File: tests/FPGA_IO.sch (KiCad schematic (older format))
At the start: 9 parts, among them U4 iCE40-HX8K-CT256, U7 100 MHz Osc

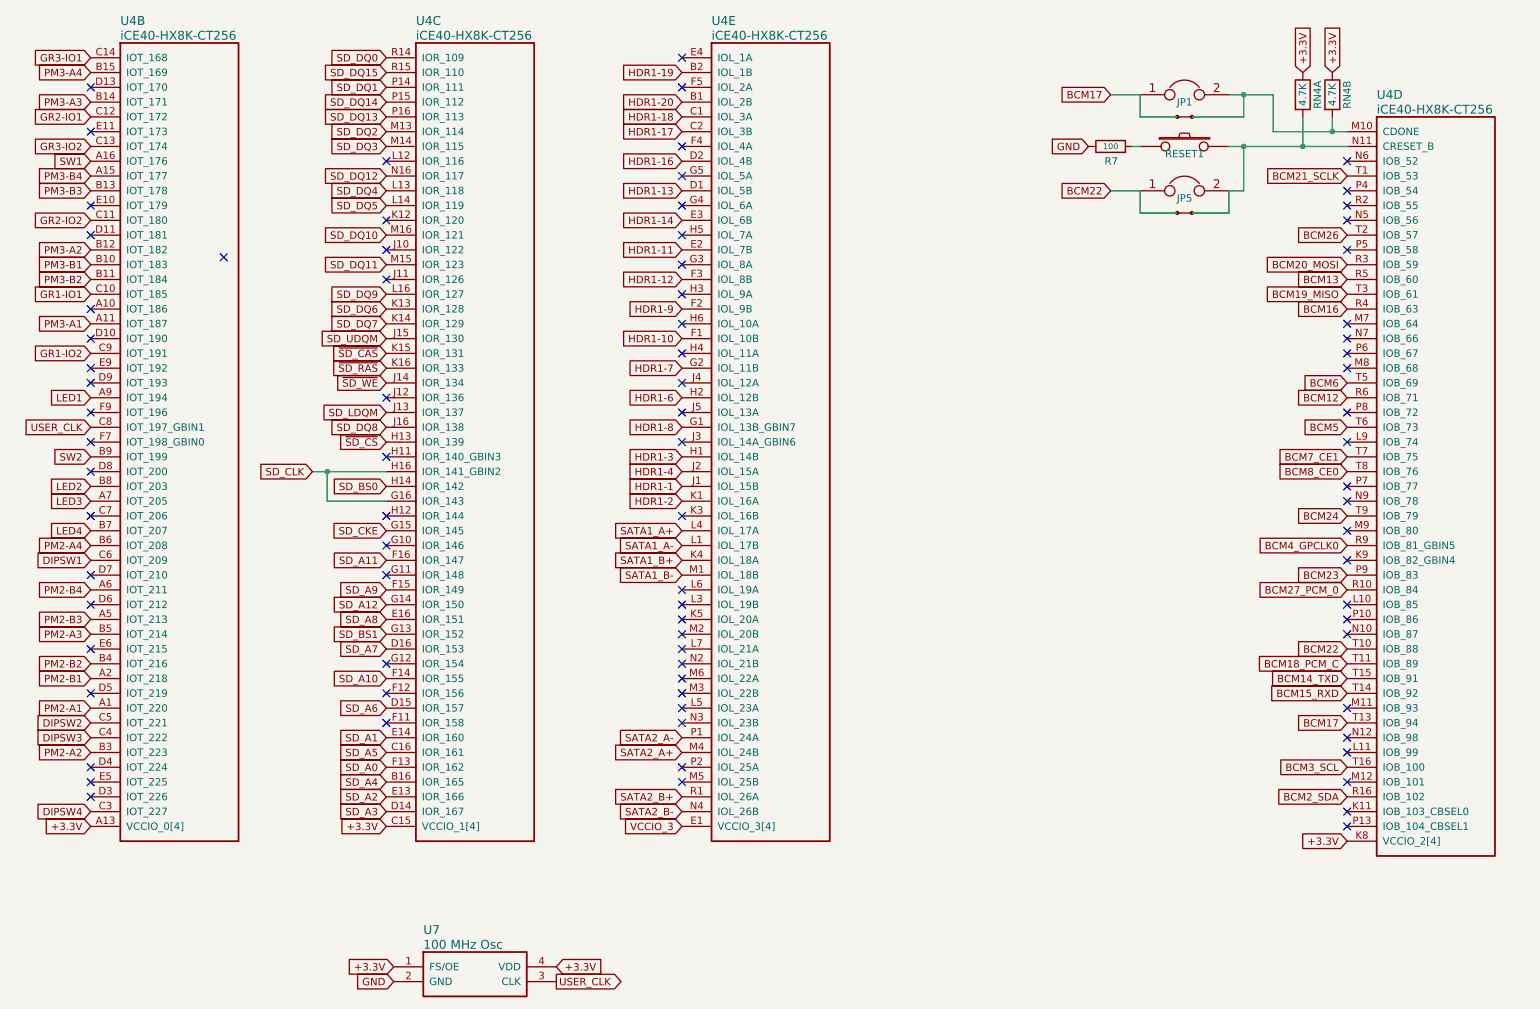
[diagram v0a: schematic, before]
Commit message: Added recursive operations on hierarchical schematics.
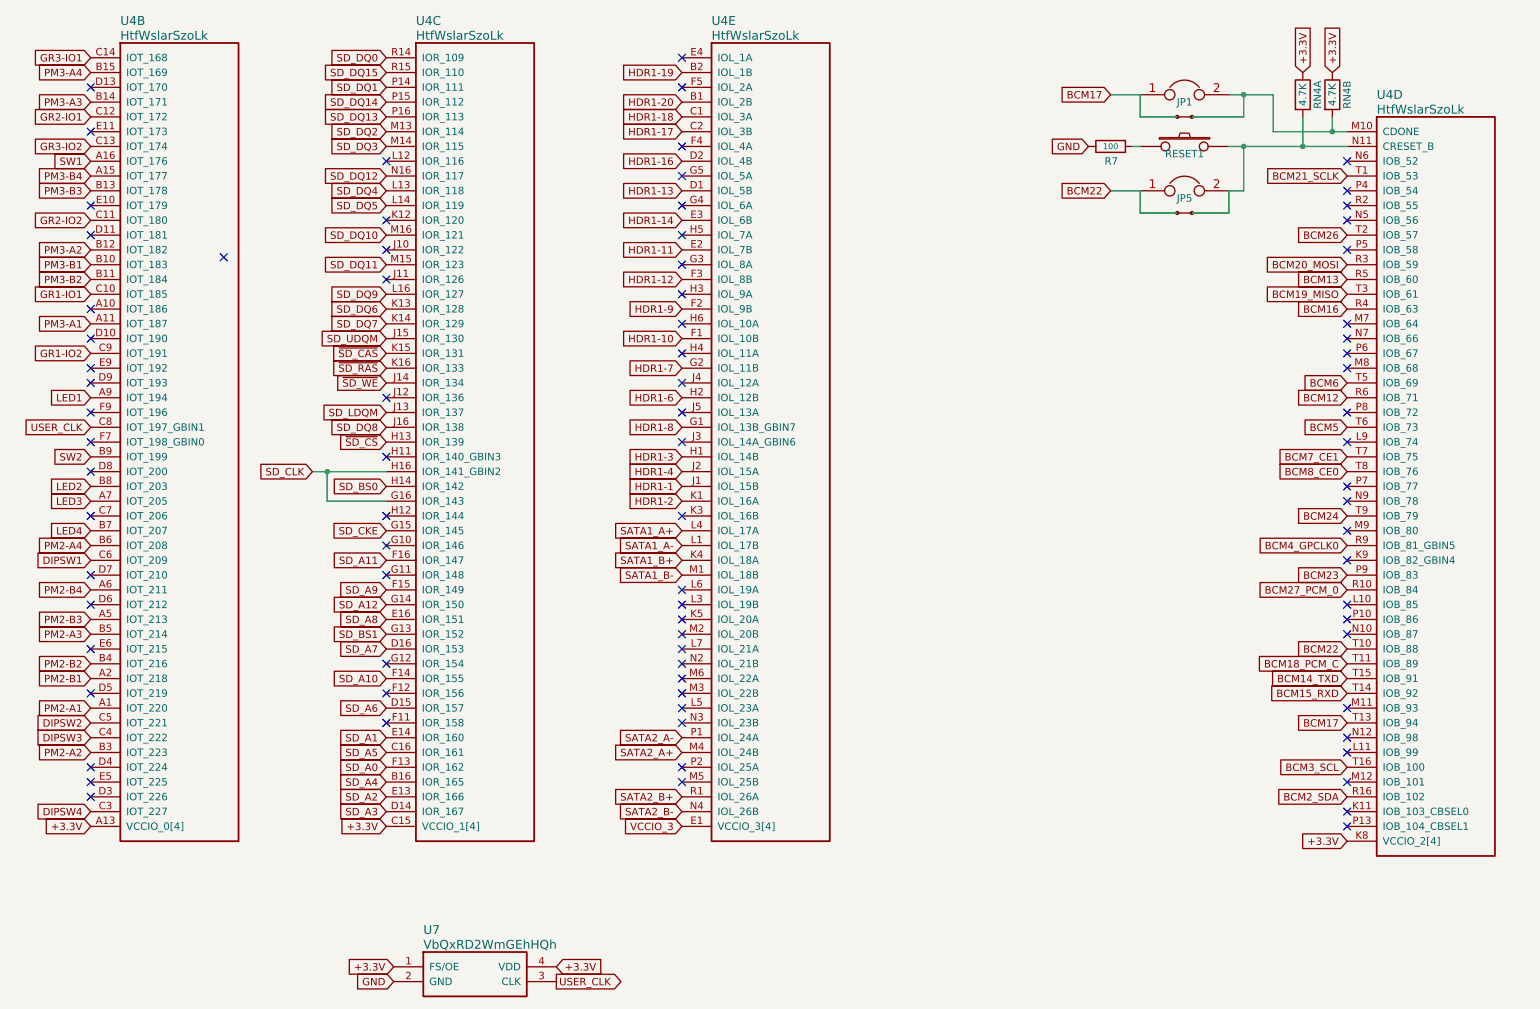
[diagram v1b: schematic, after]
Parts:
- JP1: manf (none) -> ZDgNoeyb2BY1ILy8
- R7: manf (none) -> f1oXAayzedLD07Gj; zzzDXp9J5Qc (none) -> cYjMJdJOgHt9wRNhr; zzzkoq (none) -> Vkv28aGm
- RN4: manf (none) -> mRbGBWMKorEoeWPpgQ; manf# (none) -> xl3iO2lQG6DrO3
- SH5: value JSHORTNORMAL -> 0tF4LilnkuNbdFueI; footprint XESS:xess-JSHORT -> RbT021YhlS24
- SH6: manf# (none) -> 4y822ed8; zzzDXp9J5Qc (none) -> n21qZ
- U4: value iCE40-HX8K-CT256 -> HtfWslarSzoLk; manf# (none) -> HiyQG6ncOK
- U7: value 100 MHz Osc -> VbQxRD2WmGEhHQh; manf (none) -> 76Byc9bxs5Vvk6Ao; zzzDXp9J5Qc (none) -> 7lSoG9vp0YDK7ujZO
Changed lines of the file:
@@
 AR Path="/55F04D7F" Ref="U?" Part="2"
 F 0 "U4" H 1600 1150 60 0000 L CNN
-F 1 "iCE40-HX8K-CT256" H 1600 1050 60 0000 L CNN
+F 1 "HtfWslarSzoLk" H 1600 1050 60 0000 L CNN
 F 2 "XESS:Lattice_caBGA_256" H 1400 900 60 0001 C CNN
 F 3 "" H 1400 900 60 0000 C CNN
+F 4 "HiyQG6ncOK" H 0 0 50 0001 C CNN "manf#"
 	2    1400 900
 	1    0    0    -1
@@
 AR Path="/55F04D86" Ref="U?" Part="3"
 F 0 "U4" H 3600 1150 60 0000 L CNN
-F 1 "iCE40-HX8K-CT256" H 3600 1050 60 0000 L CNN
+F 1 "HtfWslarSzoLk" H 3600 1050 60 0000 L CNN
 F 2 "XESS:Lattice_caBGA_256" H 3400 900 60 0001 C CNN
 F 3 "" H 3400 900 60 0000 C CNN
+F 4 "HiyQG6ncOK" H 0 0 50 0001 C CNN "manf#"
 	3    3400 900
 	1    0    0    -1
@@
 AR Path="/55F04D8D" Ref="U?" Part="4"
 F 0 "U4" H 10100 1650 60 0000 L CNN
-F 1 "iCE40-HX8K-CT256" H 10100 1550 60 0000 L CNN
+F 1 "HtfWslarSzoLk" H 10100 1550 60 0000 L CNN
 F 2 "XESS:Lattice_caBGA_256" H 9900 1400 60 0001 C CNN
 F 3 "" H 9900 1400 60 0000 C CNN
+F 4 "HiyQG6ncOK" H 0 0 50 0001 C CNN "manf#"
 	4    9900 1400
 	1    0    0    -1
@@
 AR Path="/55F04D94" Ref="U?" Part="5"
 F 0 "U4" H 5600 1150 60 0000 L CNN
-F 1 "iCE40-HX8K-CT256" H 5600 1050 60 0000 L CNN
+F 1 "HtfWslarSzoLk" H 5600 1050 60 0000 L CNN
 F 2 "XESS:Lattice_caBGA_256" H 5400 900 60 0001 C CNN
 F 3 "" H 5400 900 60 0000 C CNN
+F 4 "HiyQG6ncOK" H 0 0 50 0001 C CNN "manf#"
 	5    5400 900
 	1    0    0    -1
@@
 P 3450 7050
 F 0 "U7" H 3650 7300 60 0000 L CNN
-F 1 "100 MHz Osc" H 3650 7200 60 0000 L CNN
+F 1 "VbQxRD2WmGEhHQh" H 3650 7200 60 0000 L CNN
 F 2 "XESS:2.5x3.2" H 3450 7050 50 0001 C CNN
 F 3 "" H 3450 7050 50 0000 C CNN
-F 4 "501ACA100M000CAG" H 3450 7050 60 0001 C CNN "manf#"
-F 5 "" H 0 0 50 0001 C CNN "manf"
+F 4 "76Byc9bxs5Vvk6Ao" H 0 0 50 0001 C CNN "manf"
+F 5 "501ACA100M000CAG" H 3450 7050 60 0001 C CNN "manf#"
+F 6 "7lSoG9vp0YDK7ujZO" H 0 0 50 0001 C CNN "zzzDXp9J5Qc"
 	1    3450 7050
 	1    0    0    -1
@@
 F 2 "XESS:CTS_742C043" H 9600 1300 50 0001 C CNN
 F 3 "" H 9600 1300 50 0000 C CNN
-F 4 "" H 0 0 50 0001 C CNN "manf#"
-F 5 "" H 0 0 50 0001 C CNN "manf"
+F 4 "mRbGBWMKorEoeWPpgQ" H 0 0 50 0001 C CNN "manf"
+F 5 "xl3iO2lQG6DrO3" H 0 0 50 0001 C CNN "manf#"
 	1    9600 1300
 	0    -1   -1   0
@@
 F 2 "XESS:CTS_742C043" H 9800 1300 50 0001 C CNN
 F 3 "" H 9800 1300 50 0000 C CNN
-F 4 "" H 0 0 50 0001 C CNN "manf#"
-F 5 "" H 0 0 50 0001 C CNN "manf"
+F 4 "mRbGBWMKorEoeWPpgQ" H 0 0 50 0001 C CNN "manf"
+F 5 "xl3iO2lQG6DrO3" H 0 0 50 0001 C CNN "manf#"
 	2    9800 1300
 	0    -1   -1   0
@@
 F 2 "XESS:RS-282G05A3-SM_RT" H 8800 1500 60 0001 C CNN
 F 3 "" H 8800 1500 60 0000 C CNN
-F 4 "" H 0 0 50 0001 C CNN "manf#"
-F 5 "" H 0 0 50 0001 C CNN "manf"
 	1    8800 1500
 	1    0    0    -1
@@
 F 2 "XESS:S_JUMPER_2" H 8800 1800 60 0001 C CNN
 F 3 "" H 8800 1800 60 0000 C CNN
-F 4 "" H 0 0 50 0001 C CNN "manf#"
-F 5 "" H 0 0 50 0001 C CNN "manf"
 	1    8800 1800
 	1    0    0    -1
@@
 F 2 "XESS:S_JUMPER_2" H 8800 1150 60 0001 C CNN
 F 3 "" H 8800 1150 60 0000 C CNN
-F 4 "" H 0 0 50 0001 C CNN "manf#"
-F 5 "" H 0 0 50 0001 C CNN "manf"
+F 4 "ZDgNoeyb2BY1ILy8" H 0 0 50 0001 C CNN "manf"
 	1    8800 1150
 	1    0    0    -1
@@
 AR Path="/55DF5F27/55E883EA/55F049F2/55F913D4" Ref="SH5" Part="1"
 F 0 "SH5" H 8850 1200 50 0001 L BNN
-F 1 "JSHORTNORMAL" H 8750 1200 50 0001 L BNN
-F 2 "XESS:xess-JSHORT" H 8850 1450 50 0001 C CNN
+F 1 "0tF4LilnkuNbdFueI" H 8750 1200 50 0001 L BNN
+F 2 "RbT021YhlS24" H 8850 1450 50 0001 C CNN
 F 3 "" H 8850 1300 60 0000 C CNN
 	1    8850 1300
@@
 F 2 "XESS:xess-JSHORT" H 8850 2100 50 0001 C CNN
 F 3 "" H 8850 1950 60 0000 C CNN
+F 4 "4y822ed8" H 0 0 50 0001 C CNN "manf#"
+F 5 "n21qZ" H 0 0 50 0001 C CNN "zzzDXp9J5Qc"
 	1    8850 1950
 	-1   0    0    1
@@
 F 2 "Resistors_SMD:R_0603" H 8300 1500 60 0001 C CNN
 F 3 "" H 8300 1500 60 0000 C CNN
-F 4 "RC0603JR-07100RL" V 8300 1500 60 0001 C CNN "manf#"
-F 5 "" H 0 0 50 0001 C CNN "manf"
+F 4 "f1oXAayzedLD07Gj" H 0 0 50 0001 C CNN "manf"
+F 5 "RC0603JR-07100RL" V 8300 1500 60 0001 C CNN "manf#"
+F 6 "cYjMJdJOgHt9wRNhr" H 0 0 50 0001 C CNN "zzzDXp9J5Qc"
+F 7 "Vkv28aGm" H 0 0 50 0001 C CNN "zzzkoq"
 	1    8300 1500
 	0    -1   -1   0
